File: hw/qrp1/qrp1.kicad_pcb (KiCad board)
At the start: 2 copper layers, 100 x 35 mm, 45 parts, among them J1 Conn_Coaxial, J2 Conn_Coaxial, J3 Conn_01x02, J4 Conn_01x02, Q1 2N3904, Q2 2N2219, T1 Bifilar Toroid, T2 Bifilar Toroid, U1 MC78L06_TO92, U2 IRF510PBF

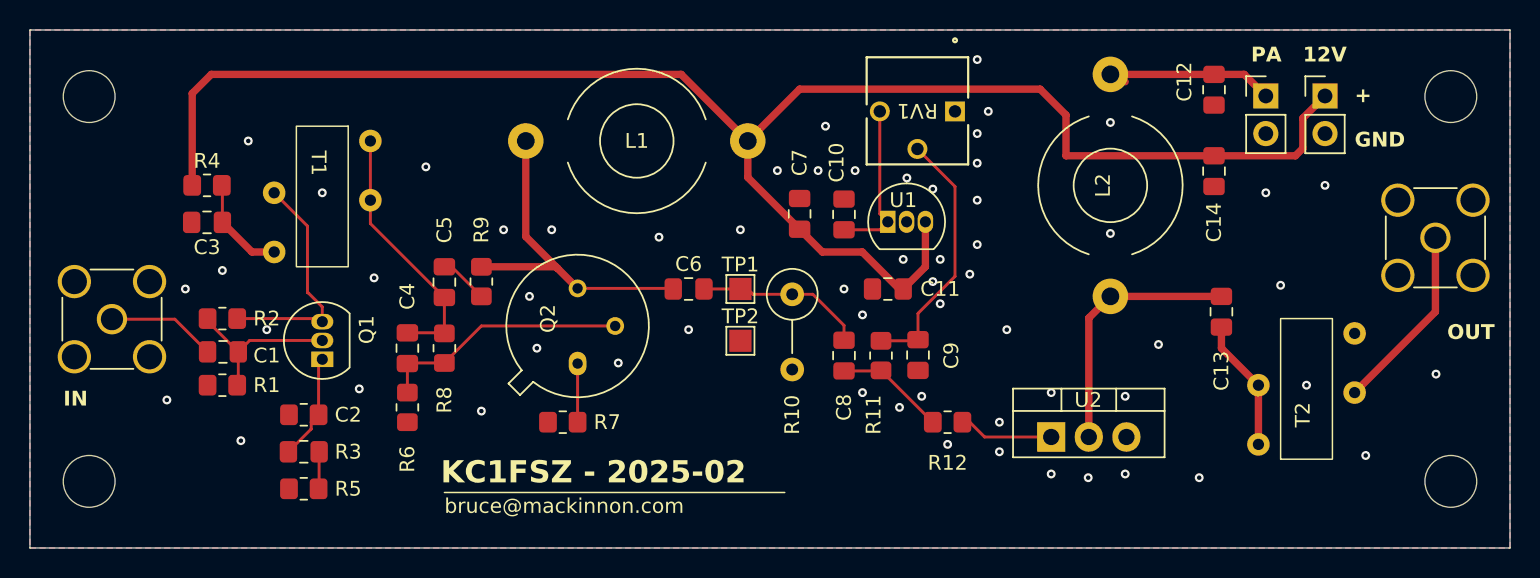
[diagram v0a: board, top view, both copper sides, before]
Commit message: Added power enable control on driver stages
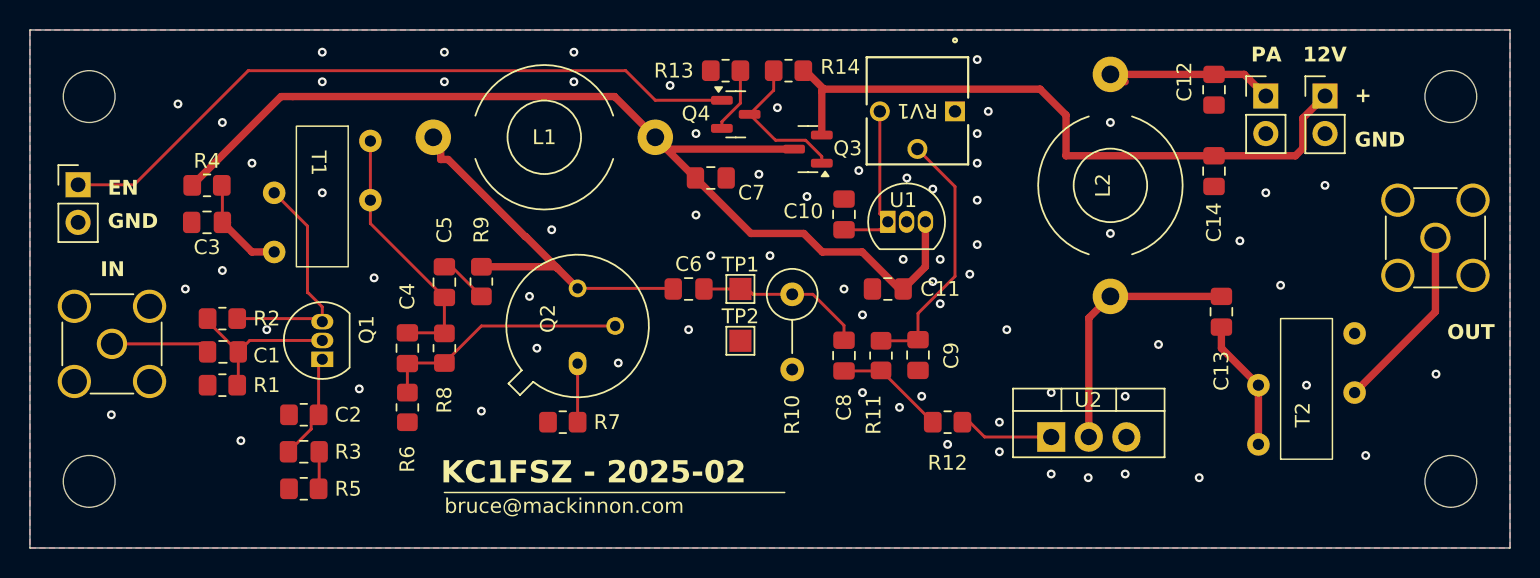
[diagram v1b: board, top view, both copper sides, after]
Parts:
- added J5: Conn_01x02, Connector_PinHeader_2.54mm:PinHeader_1x02_P2.54mm_Vertical, F.Cu at (106.2, 80.5)
- added Q3: FDN340P, Package_TO_SOT_SMD:SOT-23, F.Cu at (155.6, 78.0)
- added Q4: MMBT3904, Package_TO_SOT_SMD:SOT-23, F.Cu at (150.7, 75.7)
- added R13: 2.2k, Resistor_SMD:R_0805_2012Metric_Pad1.20x1.40mm_HandSolder, F.Cu at (150.0, 72.8)
- added R14: 10k, Resistor_SMD:R_0805_2012Metric_Pad1.20x1.40mm_HandSolder, F.Cu at (154.2, 72.8)
- moved C7 6.47 mm to (149.0, 80.0), turned to 0 degrees
- moved L1 6.25 mm to (145.2, 77.2)
- moved J1 1.67 mm to (108.5, 91.2)
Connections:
- C11 pad 1: +12V -> +12V_SWITCHED
- C7 pad 1: +12V -> +12V_SWITCHED
- L1 pad 1: +12V -> +12V_SWITCHED
- R4 pad 1: +12V -> +12V_SWITCHED
- U1 pad 3: +12V -> +12V_SWITCHED
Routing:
- net +12V_SWITCHED: track 0.00 -> 70.9 mm
- net +12V: track 114.6 -> 45.6 mm
- net ~{EN}: track 0.00 -> 47.5 mm
- net Net-(Q3-G): track 0.00 -> 10.1 mm
- net Net-(Q4-E): track 0.00 -> 4.42 mm
- net Net-(Q2-C): track 23.1 -> 26.2 mm
- net Net-(J1-In): track 7.38 -> 6.68 mm
- net GND: vias 60 -> 70
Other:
- board text added: "EN"

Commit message: Sending QRP PA/LPF boards to JLC
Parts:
- moved J2 8.96 mm to (198.0, 93.0)
- moved T2 1.50 mm to (187.5, 94.0)
- moved C7 1.41 mm to (150.0, 81.0)
- moved H1 0.50 mm to (107.0, 74.0)
- moved H2 0.50 mm to (107.0, 101.0)
- moved H3 0.50 mm to (199.0, 74.0)
- moved H4 0.50 mm to (199.0, 101.0)
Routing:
- net Net-(J2-In): track 12.7 -> 6.77 mm
- net Net-(T2-AA): track 8.96 -> 8.34 mm
- net GND: vias 70 -> 71
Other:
- board text added: "KC1FSZ 2025-02"
- board text removed: "KC1FSZ - 2025-02"
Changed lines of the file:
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@@
 		(tags "resistor handsolder")
 		(property "Reference" "R13"
-			(at 3.5 0 360)
+			(at 3.5 0 0)
 			(layer "F.SilkS")
 			(effects
@@
 		)
 		(property "Value" "2.2k"
-			(at 0 1.65 360)
+			(at 0 1.65 0)
 			(layer "F.Fab")
 			(effects
@@
 		)
 		(fp_text user "${REFERENCE}"
-			(at 0 0 360)
+			(at 0 0 0)
 			(layer "F.Fab")
 			(effects
@@
 		(tags "Through hole pin header THT 1x02 2.54mm single row")
 		(property "Reference" "J5"
-			(at 0 -2.33 360)
+			(at 0 -2.33 0)
 			(layer "F.SilkS")
 			(hide yes)
@@
 		)
 		(property "Value" "Conn_01x02"
-			(at 0 4.87 360)
+			(at 0 4.87 0)
 			(layer "F.Fab")
 			(effects
@@
 	(footprint "MountingHole:MountingHole_3.5mm"
 		(layer "F.Cu")
-		(at 199 100.5)
+		(at 199 101)
 		(descr "Mounting Hole 3.5mm, no annular")
 		(tags "mounting hole 3.5mm no annular")
@@
 	(footprint "Capacitor_SMD:C_0805_2012Metric_Pad1.18x1.45mm_HandSolder"
 		(layer "F.Cu")
-		(at 149 80)
+		(at 150 81)
 		(descr "Capacitor SMD 0805 (2012 Metric), square (rectangular) end terminal, IPC_7351 nominal with elongated pad for handsoldering. (Body size source: IPC-SM-782 page 76, https://www.pcb-3d.com/wordpress/wp-content/uploads/ipc-sm-782a_amendment_1_and_2.pdf, https://docs.google.com/spreadsheets/d/1BsfQQcO9C6DZCsRaXUlFlo91Tg2WpOkGARC1WS5S8t0/edit?usp=sharing), generated with kicad-footprint-generator")
 		(tags "capacitor handsolder")
 		(property "Reference" "C7"
-			(at 2.75 1 360)
+			(at 2.75 1 0)
 			(layer "F.SilkS")
 			(effects
@@
 		)
 		(property "Value" "0.1uF"
-			(at 0 1.68 360)
+			(at 0 1.68 0)
 			(layer "F.Fab")
 			(effects
@@
 		)
 		(fp_text user "${REFERENCE}"
-			(at 0 0 360)
+			(at 0 0 0)
 			(layer "F.Fab")
 			(effects
@@
 		(tags "resistor handsolder")
 		(property "Reference" "R14"
-			(at -3.5 0.25 360)
+			(at -3.5 0.25 0)
 			(layer "F.SilkS")
 			(effects
@@
 		)
 		(property "Value" "10k"
-			(at 0 1.65 360)
+			(at 0 1.65 0)
 			(layer "F.Fab")
 			(effects
@@
 		)
 		(fp_text user "${REFERENCE}"
-			(at 0 0 360)
+			(at 0 0 0)
 			(layer "F.Fab")
 			(effects
@@
 		(tags "SOT TO_SOT_SMD")
 		(property "Reference" "Q3"
-			(at -2.6875 0.05 360)
+			(at -2.6875 0.05 0)
 			(layer "F.SilkS")
 			(effects
@@
 		)
 		(property "Value" "FDN340P"
-			(at 0 2.4 360)
+			(at 0 2.4 0)
 			(layer "F.Fab")
 			(effects
@@
 		)
 		(fp_text user "${REFERENCE}"
-			(at 0 0 360)
+			(at 0 0 0)
 			(layer "F.Fab")
 			(effects
@@
 	(footprint "MountingHole:MountingHole_3.5mm"
 		(layer "F.Cu")
-		(at 107 100.5)
+		(at 107 101)
 		(descr "Mounting Hole 3.5mm, no annular")
 		(tags "mounting hole 3.5mm no annular")
@@
 		(tags "capacitor handsolder")
 		(property "Reference" "C13"
-			(at 4 0 90)
+			(at 3.7125 1.75 90)
 			(layer "F.SilkS")
 			(effects
@@
 	(footprint "bruce-footprints:FT37-43 Bifilar"
 		(layer "F.Cu")
-		(at 189 94 90)
+		(at 187.5 94 90)
 		(property "Reference" "T2"
 			(at -2 0 90)
@@
 	(footprint "MountingHole:MountingHole_3.5mm"
 		(layer "F.Cu")
-		(at 199 74.5)
+		(at 199 74)
 		(descr "Mounting Hole 3.5mm, no annular")
 		(tags "mounting hole 3.5mm no annular")
@@
 	(footprint "MountingHole:MountingHole_3.5mm"
 		(layer "F.Cu")
-		(at 107 74.5)
+		(at 107 74)
 		(descr "Mounting Hole 3.5mm, no annular")
 		(tags "mounting hole 3.5mm no annular")
@@
 	(footprint "Connector_Coaxial:SMA_Amphenol_901-144_Vertical"
 		(layer "F.Cu")
-		(at 197.96 84.04)
+		(at 197.96 93)
 		(descr "https://www.amphenolrf.com/downloads/dl/file/id/7023/product/3103/901_144_customer_drawing.pdf")
 		(tags "SMA THT Female Jack Vertical")
@@
 	(gr_line
 		(start 131 101.25)
-		(end 154 101.25)
+		(end 151.25 101.25)
 		(stroke
 			(width 0.1)
@@
 		)
 	)
-	(gr_text "KC1FSZ - 2025-02"
+	(gr_text "KC1FSZ 2025-02"
 		(at 130.75 100.75 0)
 		(layer "F.SilkS")
@@
 	)
 	(gr_text "OUT"
-		(at 198.75 91 0)
+		(at 196.75 88 0)
 		(layer "F.SilkS")
 		(effects
@@
 		)
 	)
+	(dimension
+		(type aligned)
+		(layer "Dwgs.User")
+		(pts
+			(xy 107 101) (xy 107 105)
+		)
+		(height 8)
+		(gr_text "4.0000 mm"
+			(at 97.85 103 90)
+			(layer "Dwgs.User")
+			(effects
+				(font
+					(size 1 1)
+					(thickness 0.15)
+				)
+			)
+		)
+		(format
+			(prefix "")
+			(suffix "")
+			(units 3)
+			(units_format 1)
+			(precision 4)
+		)
+		(style
+			(thickness 0.1)
+			(arrow_length 1.27)
+			(text_position_mode 0)
+			(extension_height 0.58642)
+			(extension_offset 0.5) keep_text_aligned)
+	)
+	(dimension
+		(type aligned)
+		(layer "Dwgs.User")
+		(pts
+			(xy 204 105) (xy 204 93)
+		)
+		(height 3)
+		(gr_text "12.0000 mm"
+			(at 205.85 99 90)
+			(layer "Dwgs.User")
+			(effects
+				(font
+					(size 1 1)
+					(thickness 0.15)
+				)
+			)
+		)
+		(format
+			(prefix "")
+			(suffix "")
+			(units 3)
+			(units_format 1)
+			(precision 4)
+		)
+		(style
+			(thickness 0.1)
+			(arrow_length 1.27)
+			(text_position_mode 0)
+			(extension_height 0.58642)
+			(extension_offset 0.5) keep_text_aligned)
+	)
+	(dimension
+		(type aligned)
+		(layer "Dwgs.User")
+		(pts
+			(xy 107 101) (xy 103 101)
+		)
+		(height -10)
+		(gr_text "4.0000 mm"
+			(at 105 109.85 0)
+			(layer "Dwgs.User")
+			(effects
+				(font
+					(size 1 1)
+					(thickness 0.15)
+				)
+			)
+		)
+		(format
+			(prefix "")
+			(suffix "")
+			(units 3)
+			(units_format 1)
+			(precision 4)
+		)
+		(style
+			(thickness 0.1)
+			(arrow_length 1.27)
+			(text_position_mode 0)
+			(extension_height 0.58642)
+			(extension_offset 0.5) keep_text_aligned)
+	)
+	(dimension
+		(type aligned)
+		(layer "Dwgs.User")
+		(pts
+			(xy 103 70) (xy 203 70)
+		)
+		(height -6)
+		(gr_text "100.0000 mm"
+			(at 153 62.85 0)
+			(layer "Dwgs.User")
+			(effects
+				(font
+					(size 1 1)
+					(thickness 0.15)
+				)
+			)
+		)
+		(format
+			(prefix "")
+			(suffix "")
+			(units 3)
+			(units_format 1)
+			(precision 4)
+		)
+		(style
+			(thickness 0.1)
+			(arrow_length 1.27)
+			(text_position_mode 0)
+			(extension_height 0.58642)
+			(extension_offset 0.5) keep_text_aligned)
+	)
+	(dimension
+		(type aligned)
+		(layer "Dwgs.User")
+		(pts
+			(xy 204 105) (xy 204 70)
+		)
+		(height 6)
+		(gr_text "35.0000 mm"
+			(at 208.85 87.5 90)
+			(layer "Dwgs.User")
+			(effects
+				(font
+					(size 1 1)
+					(thickness 0.15)
+				)
+			)
+		)
+		(format
+			(prefix "")
+			(suffix "")
+			(units 3)
+			(units_format 1)
+			(precision 4)
+		)
+		(style
+			(thickness 0.1)
+			(arrow_length 1.27)
+			(text_position_mode 0)
+			(extension_height 0.58642)
+			(extension_offset 0.5) keep_text_aligned)
+	)
 	(segment
 		(start 108.54 91.21)
@@
 	)
 	(via
-		(at 198 93.25)
+		(at 119 90.25)
 		(size 0.6)
 		(drill 0.3)
@@
 	)
 	(via
-		(at 119 90.25)
+		(at 195 87)
+		(size 0.6)
+		(drill 0.3)
+		(layers "F.Cu" "B.Cu")
+		(free yes)
+		(net 5)
+	)
+	(via
+		(at 201 87)
 		(size 0.6)
 		(drill 0.3)
@@
 	)
 	(via
-		(at 152.25 79.75)
+		(at 153 80)
 		(size 0.6)
 		(drill 0.3)
@@
 	)
 	(segment
+		(start 184.5 94)
+		(end 184.5 92.5)
+		(width 0.5)
+		(layer "F.Cu")
+		(net 16)
+	)
+	(segment
 		(start 183.5 90.075)
 		(end 183.5 91.5)
@@
 	)
 	(segment
-		(start 186 94)
-		(end 186 98)
+		(start 184.5 94)
+		(end 184.5 98)
 		(width 0.5)
 		(layer "F.Cu")
@@
 	)
 	(segment
-		(start 183.5 91.5)
-		(end 186 94)
+		(start 184.5 92.5)
+		(end 183.5 91.5)
 		(width 0.5)
 		(layer "F.Cu")
@@
 	)
 	(segment
-		(start 197.96 89.04)
-		(end 197.96 84.04)
+		(start 191 94.5)
+		(end 192.5 93)
 		(width 0.5)
 		(layer "F.Cu")
@@
 	)
 	(segment
-		(start 192.5 94.5)
-		(end 197.96 89.04)
+		(start 192.5 93)
+		(end 197.15 93)
 		(width 0.5)
 		(layer "F.Cu")
